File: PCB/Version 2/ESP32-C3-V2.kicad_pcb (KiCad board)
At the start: 4 copper layers, 27.7 x 24.3 mm, 52 parts, among them J2 DPS_PPS, J3 HCZZ0001-4, Q1 WPM2031-3/TR, SW2 TS-1187A-B-A-B, U1 USB-C-16P-SMD, U2 DS8561-33S5, U3 ESP32-C3, U4 BQ24073RGTR, U5 SKCL3130ME, Y1 40MHz_S3240000151040

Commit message: Version 2 zur Korrektur fertig
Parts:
- removed C10: 4u7_0402_X5R _10V, Capacitor_SMD:C_0402_1005Metric
- removed R20: 10k_0402, Resistor_SMD:R_0402_1005Metric
- removed R21: 3k_0402, Resistor_SMD:R_0402_1005Metric
- added C15: 10u_0402_X5R_6V3, Capacitor_SMD:C_0402_1005Metric, F.Cu at (137.6, 73.3)
- added C18: 10u_0402_X5R_6V3, Capacitor_SMD:C_0402_1005Metric, F.Cu at (133.9, 75.1)
- added D4: 1N5819WS(Basic), Diode_SMD:D_SOD-323_HandSoldering, F.Cu at (132.7, 81.6)
- added U6: MT9700, Package_TO_SOT_SMD:SOT-23-5, F.Cu at (136.5, 75.5)
- C8: value 1u_0402_X5R_25V -> 10u_0402_X5R_6V3
- C9: value 4u7_0402_X5R _10V -> 10u_0402_X5R_6V3
- R11: value 1k5_0603 -> 1k_0402; footprint Resistor_SMD:R_0603_1608Metric -> Resistor_SMD:R_0402_1005Metric
- R16: value 5k1_0402 -> 10k_0402
- R17: value 3k_0402 -> 6k8_0402
- U4: value BQ24073RGTR -> TC4056A; footprint Package_DFN_QFN:VQFN-16-1EP_3x3mm_P0.5mm_EP1.6x1.6mm -> Package_SO:SOP-8_3.9x4.9mm_P1.27mm
- moved R11 9.34 mm to (132.6, 73.2), turned to 90 degrees
- moved R17 4.18 mm to (133.4, 76.6), turned to 180 degrees
- moved C8 3.65 mm to (139.3, 85.3)
- moved D3 3.00 mm to (135.1, 73.0), turned to 180 degrees
- moved R16 2.93 mm to (137.4, 85.3), turned to 180 degrees
- moved C9 1.07 mm to (141.0, 80.7), turned to -90 degrees
- moved R5 0.86 mm to (138.1, 86.8), turned to -90 degrees
- moved U4 0.81 mm to (137.7, 81.0), turned to 90 degrees
- moved D2 0.76 mm to (130.7, 73.7)
- moved J2 0.60 mm to (143.0, 75.0)
- moved R18 0.50 mm to (134.1, 79.2)
- moved U2 0.50 mm to (131.5, 78.8)
- moved C12 0.32 mm to (133.7, 83.9)
- moved Q1 0.32 mm to (132.2, 83.9)
- moved R13 0.32 mm to (132.2, 85.4)
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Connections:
- D3 pad 2: Net-(D3-A) -> Net-(D2-A)
- R11 pad 1: Net-(U4-ILIM) -> VCC
- R11 pad 2: GND -> Net-(D2-A)
- R16 pad 1: Net-(U4-ISET) -> GND
- R16 pad 2: GND -> Net-(U4-PROG)
- R17 pad 1: Net-(D3-A) -> Net-(U6-SET)
- R17 pad 2: OUT -> GND
- U3 pad 13: NCE -> unconnected-(U3-MTDO-Pad13)
- U3 pad 16: EN2 -> unconnected-(U3-GPIO10-Pad16)
- U3 pad 19: EN1 -> unconnected-(U3-SPIHD-Pad19)
- U3 pad 20: TD -> unconnected-(U3-SPIWP-Pad20)
- U4 pad 1: Net-(U4-TS) -> unconnected-(U4-NC-Pad1)
- U4 pad 2: +BATT -> Net-(U4-PROG)
- U4 pad 3: +BATT -> GND
- U4 pad 4: NCE -> VCC
- U4 pad 5: EN2 -> +BATT
- U4 pad 6: EN1 -> Net-(D3-K)
- U4 pad 7: Net-(D3-K) -> Net-(D2-K)
- U4 pad 8: GND -> unconnected-(U4-NTC-Pad8)
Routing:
- net +BATT: track 11.8 -> 34.1 mm, vias 2 -> 1
- net EN1: track 16.1 -> 0.00 mm, vias 2 -> 0
- net VCC: track 24.4 -> 40.2 mm, vias 0 -> 2
- net EN2: track 12.8 -> 0.00 mm, vias 2 -> 0
- net NCE: track 12.3 -> 0.00 mm, vias 2 -> 0
- net TD: track 10.3 -> 0.00 mm
- net GND: track 27.6 -> 35.3 mm, vias 111 -> 94
- net EN_ADC: track 12.1 -> 15.4 mm
- net Net-(D3-K): track 3.70 -> 6.97 mm
- net Net-(D2-A): track 1.49 -> 3.83 mm
- net Net-(U4-PROG): track 0.00 -> 1.75 mm
- net OUT: track 13.8 -> 12.1 mm
- net Net-(U4-ILIM): track 1.66 -> 0.00 mm
- net Net-(U6-SET): track 0.00 -> 1.52 mm
- net Net-(D2-K): track 7.13 -> 8.57 mm
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- removed copper zone on F.Cu, net +BATT
- removed copper zone on F.Cu, net OUT

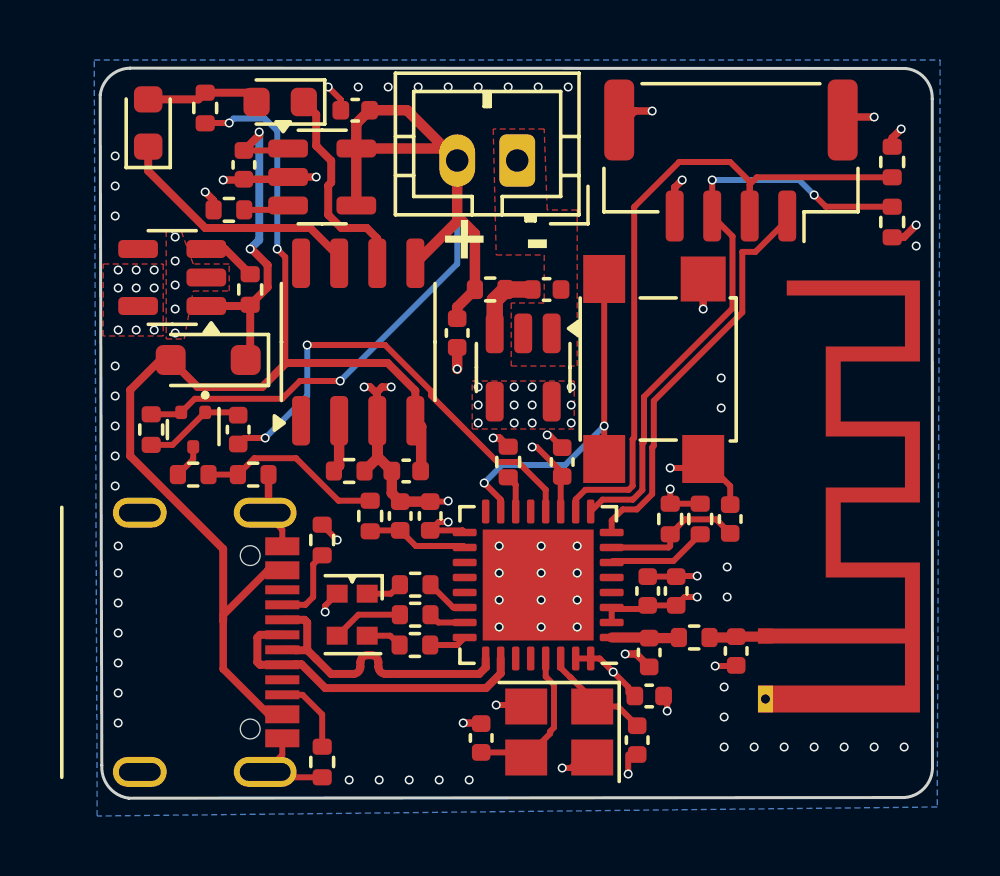
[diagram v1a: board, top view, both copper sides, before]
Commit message: Platine geprüft und überarbeitet
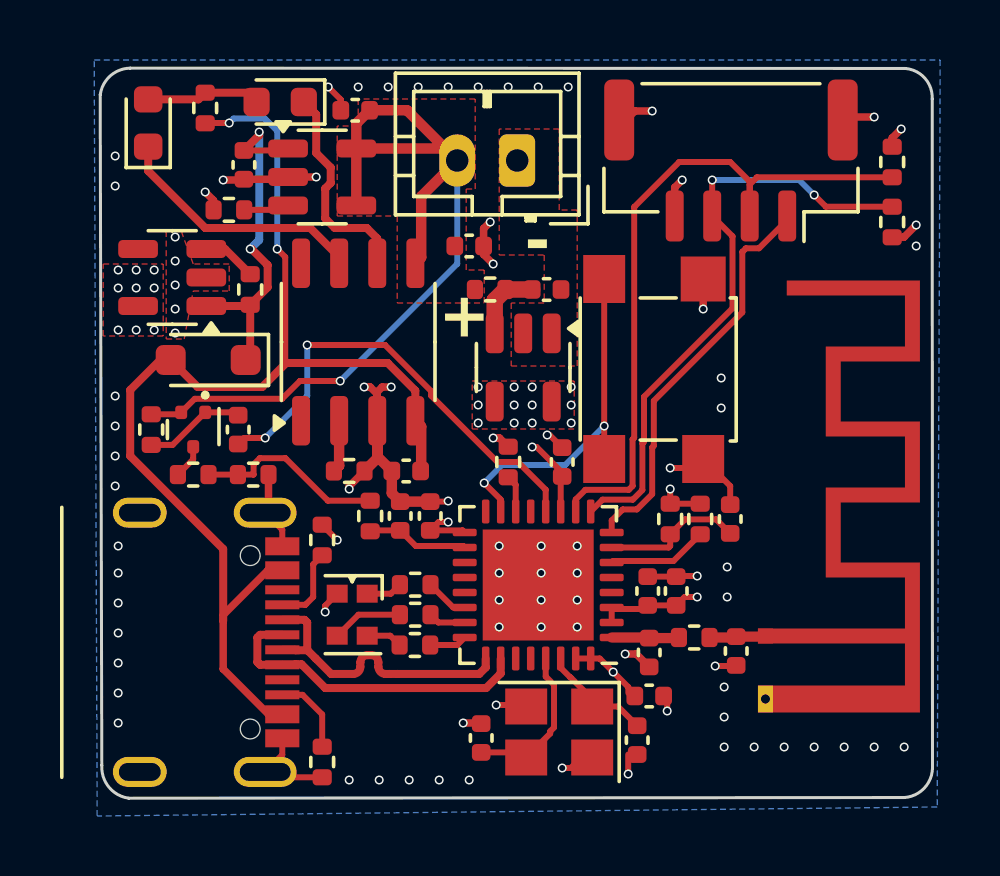
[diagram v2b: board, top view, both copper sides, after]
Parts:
- moved C9 2.93 mm to (141.4, 77.8), turned to 0 degrees
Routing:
- net +BATT: track 34.1 -> 30.2 mm
- net GND: track 35.3 -> 37.0 mm
- added copper zone on F.Cu, net +BATT
